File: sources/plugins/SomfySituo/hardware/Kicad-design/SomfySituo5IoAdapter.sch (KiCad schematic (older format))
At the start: 32 parts, among them J1 USB_OTG, J10 Conn_01x01, J11 Conn_01x01, J12 Conn_01x01, J13 Conn_01x01, J14 AVX 00-9188 006, J15 ICSP, J2 Conn_01x01, J3 Conn_01x01, J4 Conn_01x01, J5 Conn_01x01, J6 Conn_01x01, J7 Conn_01x01, J8 Conn_01x01, J9 Conn_01x01, P2 ICSP_PicKit2, U1 FT230X, U2 PIC16F688

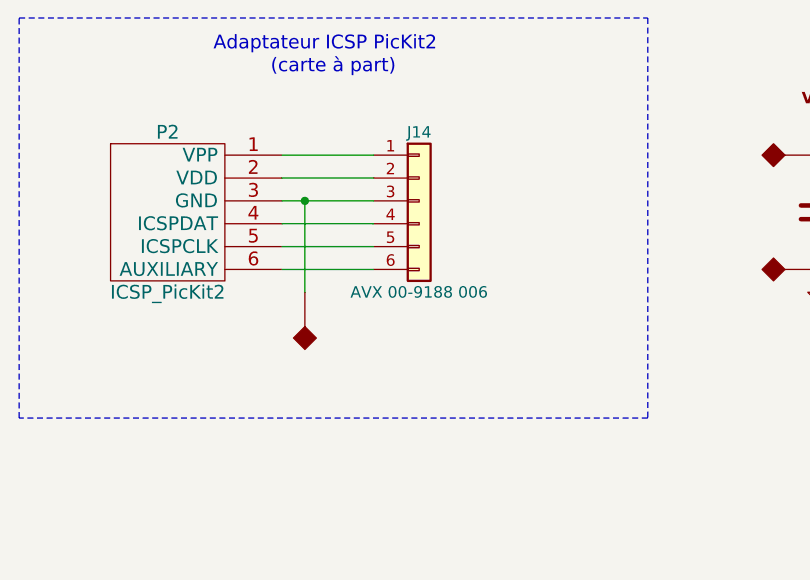
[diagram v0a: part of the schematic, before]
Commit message: Add PicKit2Adapter design (+ PCB)
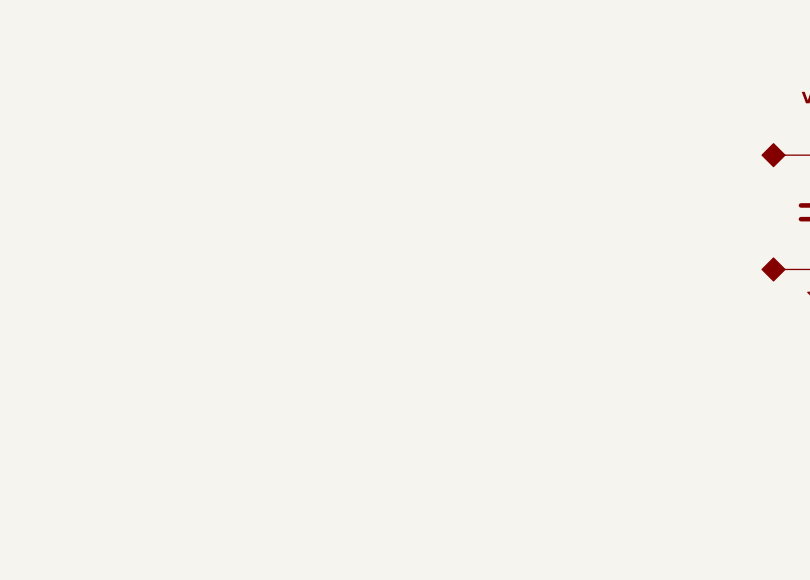
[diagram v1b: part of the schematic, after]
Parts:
- removed J14: AVX 00-9188 006, symbol Conn_01x06
- removed P2: ICSP_PicKit2, Connectors:Wafer_Horizontal17.5x5.8x7RM2.5-6, symbol ICSP_PicKit2
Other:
- note removed: "(carte à part)"
- note removed: "Adaptateur ICSP PicKit2"
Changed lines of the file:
@@
 LIBS:ESD_Protection
 LIBS:CP2102N-A01-GQFN20
-LIBS:ICSP_PicKit2
 LIBS:serial
 LIBS:SomfySituo5IoAdapter-cache
@@
 Text Label 1350 4150 0    60   ~ 0
 VCC_IN
-$Comp
-L ICSP_PicKit2 P2
-U 1 1 5AAA85AF
-P 1600 1850
-F 0 "P2" H 1450 2200 60  0000 C CNN
-F 1 "ICSP_PicKit2" H 1450 1500 60  0000 C CNN
-F 2 "Connectors:Wafer_Horizontal17.5x5.8x7RM2.5-6" H 1600 1850 60  0001 C CNN
-F 3 "" H 1600 1850 60  0001 C CNN
-	1    1600 1850
-	1    0    0    -1
-$EndComp
-Text Notes 1650 1150 0    60   ~ 0
-Adaptateur ICSP PicKit2
-Text Notes 1900 1250 0    60   ~ 0
-(carte à part)
-$Comp
-L Conn_01x06 J14
-U 1 1 5AAA8FB8
-P 2550 1800
-F 0 "J14" H 2550 2100 50  0000 C CNN
-F 1 "AVX 00-9188 006" H 2550 1400 50  0000 C CNN
-F 2 "" H 2550 1800 50  0001 C CNN
-F 3 "" H 2550 1800 50  0001 C CNN
-	1    2550 1800
-	1    0    0    -1
-$EndComp
 Wire Wire Line
 	1000 4750 1000 4850
@@
 Wire Wire Line
 	8500 1550 8800 1550
-Wire Notes Line
-	800  1000 3550 1000
-Wire Notes Line
-	3550 1000 3550 2750
-Wire Notes Line
-	3550 2750 800  2750
-Wire Notes Line
-	800  2750 800  1000
-Wire Wire Line
-	1950 1600 2350 1600
-Wire Wire Line
-	2350 1700 1950 1700
-Wire Wire Line
-	1950 1800 2350 1800
-Wire Wire Line
-	2350 1900 1950 1900
-Wire Wire Line
-	1950 2000 2350 2000
-Wire Wire Line
-	2350 2100 1950 2100
-$Comp
-L PWR_FLAG #FLG2
-U 1 1 5AAA9696
-P 2050 2200
-F 0 "#FLG2" H 2050 2500 60  0001 C CNN
-F 1 "PWR_FLAG" H 2050 2150 40  0001 C CNN
-F 2 "" H 1950 2400 60  0001 C CNN
-F 3 "" H 2050 2500 60  0001 C CNN
-	1    2050 2200
-	-1   0    0    1
-$EndComp
-Wire Wire Line
-	2050 2200 2050 1800
-Connection ~ 2050 1800
 $Comp
 L Conn_01x06 J15

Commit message: Place components
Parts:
- J10, J11, J12, J13, J2, J3, J4, J5, J6, J7, J8, J9: footprint Socket_Strips:Socket_Strip_Straight_1x01_Pitch2.54mm -> Measurement_Points:Measurement_Point_Square-SMD-Pad_Big
- J15: footprint (none) -> AVX 00-9188 006 receiver:AVX_00-9188_006_receiver
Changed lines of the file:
@@
 F 0 "J2" H 9100 1450 50  0000 C CNN
 F 1 "Conn_01x01" H 9450 1450 50  0000 C CNN
-F 2 "Socket_Strips:Socket_Strip_Straight_1x01_Pitch2.54mm" H 9000 1450 50  0001 C CNN
+F 2 "Measurement_Points:Measurement_Point_Square-SMD-Pad_Big" H 9000 1450 50  0001 C CNN
 F 3 "" H 9000 1450 50  0001 C CNN
 	1    9000 1450
@@
 F 0 "J3" H 9100 1550 50  0000 C CNN
 F 1 "Conn_01x01" H 9450 1550 50  0000 C CNN
-F 2 "Socket_Strips:Socket_Strip_Straight_1x01_Pitch2.54mm" H 9000 1550 50  0001 C CNN
+F 2 "Measurement_Points:Measurement_Point_Square-SMD-Pad_Big" H 9000 1550 50  0001 C CNN
 F 3 "" H 9000 1550 50  0001 C CNN
 	1    9000 1550
@@
 F 0 "J4" H 9100 1650 50  0000 C CNN
 F 1 "Conn_01x01" H 9450 1650 50  0000 C CNN
-F 2 "Socket_Strips:Socket_Strip_Straight_1x01_Pitch2.54mm" H 9000 1650 50  0001 C CNN
+F 2 "Measurement_Points:Measurement_Point_Square-SMD-Pad_Big" H 9000 1650 50  0001 C CNN
 F 3 "" H 9000 1650 50  0001 C CNN
 	1    9000 1650
@@
 F 0 "J5" H 9100 1750 50  0000 C CNN
 F 1 "Conn_01x01" H 9450 1750 50  0000 C CNN
-F 2 "Socket_Strips:Socket_Strip_Straight_1x01_Pitch2.54mm" H 9000 1750 50  0001 C CNN
+F 2 "Measurement_Points:Measurement_Point_Square-SMD-Pad_Big" H 9000 1750 50  0001 C CNN
 F 3 "" H 9000 1750 50  0001 C CNN
 	1    9000 1750
@@
 F 0 "J6" H 9100 1850 50  0000 C CNN
 F 1 "Conn_01x01" H 9450 1850 50  0000 C CNN
-F 2 "Socket_Strips:Socket_Strip_Straight_1x01_Pitch2.54mm" H 9000 1850 50  0001 C CNN
+F 2 "Measurement_Points:Measurement_Point_Square-SMD-Pad_Big" H 9000 1850 50  0001 C CNN
 F 3 "" H 9000 1850 50  0001 C CNN
 	1    9000 1850
@@
 F 0 "J7" H 9100 1950 50  0000 C CNN
 F 1 "Conn_01x01" H 9450 1950 50  0000 C CNN
-F 2 "Socket_Strips:Socket_Strip_Straight_1x01_Pitch2.54mm" H 9000 1950 50  0001 C CNN
+F 2 "Measurement_Points:Measurement_Point_Square-SMD-Pad_Big" H 9000 1950 50  0001 C CNN
 F 3 "" H 9000 1950 50  0001 C CNN
 	1    9000 1950
@@
 F 0 "J8" H 9100 2050 50  0000 C CNN
 F 1 "Conn_01x01" H 9450 2050 50  0000 C CNN
-F 2 "Socket_Strips:Socket_Strip_Straight_1x01_Pitch2.54mm" H 9000 2050 50  0001 C CNN
+F 2 "Measurement_Points:Measurement_Point_Square-SMD-Pad_Big" H 9000 2050 50  0001 C CNN
 F 3 "" H 9000 2050 50  0001 C CNN
 	1    9000 2050
@@
 F 0 "J9" H 9100 2150 50  0000 C CNN
 F 1 "Conn_01x01" H 9450 2150 50  0000 C CNN
-F 2 "Socket_Strips:Socket_Strip_Straight_1x01_Pitch2.54mm" H 9000 2150 50  0001 C CNN
+F 2 "Measurement_Points:Measurement_Point_Square-SMD-Pad_Big" H 9000 2150 50  0001 C CNN
 F 3 "" H 9000 2150 50  0001 C CNN
 	1    9000 2150
@@
 F 0 "J10" H 9100 2250 50  0000 C CNN
 F 1 "Conn_01x01" H 9450 2250 50  0000 C CNN
-F 2 "Socket_Strips:Socket_Strip_Straight_1x01_Pitch2.54mm" H 9000 2250 50  0001 C CNN
+F 2 "Measurement_Points:Measurement_Point_Square-SMD-Pad_Big" H 9000 2250 50  0001 C CNN
 F 3 "" H 9000 2250 50  0001 C CNN
 	1    9000 2250
@@
 F 0 "J11" H 9100 2350 50  0000 C CNN
 F 1 "Conn_01x01" H 9450 2350 50  0000 C CNN
-F 2 "Socket_Strips:Socket_Strip_Straight_1x01_Pitch2.54mm" H 9000 2350 50  0001 C CNN
+F 2 "Measurement_Points:Measurement_Point_Square-SMD-Pad_Big" H 9000 2350 50  0001 C CNN
 F 3 "" H 9000 2350 50  0001 C CNN
 	1    9000 2350
@@
 F 0 "J12" H 9100 2450 50  0000 C CNN
 F 1 "Conn_01x01" H 9450 2450 50  0000 C CNN
-F 2 "Socket_Strips:Socket_Strip_Straight_1x01_Pitch2.54mm" H 9000 2450 50  0001 C CNN
+F 2 "Measurement_Points:Measurement_Point_Square-SMD-Pad_Big" H 9000 2450 50  0001 C CNN
 F 3 "" H 9000 2450 50  0001 C CNN
 	1    9000 2450
@@
 $EndComp
 $Comp
-L PWR_FLAG #FLG4
+L PWR_FLAG #FLG3
 U 1 1 5A8F0A07
 P 4300 2100
-F 0 "#FLG4" H 4300 2400 60  0001 C CNN
+F 0 "#FLG3" H 4300 2400 60  0001 C CNN
 F 1 "PWR_FLAG" H 4300 2050 40  0001 C CNN
 F 2 "" H 4200 2300 60  0001 C CNN
@@
 F 0 "J13" H 9100 2550 50  0000 C CNN
 F 1 "Conn_01x01" H 9450 2550 50  0000 C CNN
-F 2 "Socket_Strips:Socket_Strip_Straight_1x01_Pitch2.54mm" H 9000 2550 50  0001 C CNN
+F 2 "Measurement_Points:Measurement_Point_Square-SMD-Pad_Big" H 9000 2550 50  0001 C CNN
 F 3 "" H 9000 2550 50  0001 C CNN
 	1    9000 2550
@@
 F 0 "J15" H 6200 2100 50  0000 C CNN
 F 1 "ICSP" H 6200 1400 50  0000 C CNN
-F 2 "" H 6200 1800 50  0001 C CNN
+F 2 "AVX 00-9188 006 receiver:AVX_00-9188_006_receiver" H 6200 1800 50  0001 C CNN
 F 3 "" H 6200 1800 50  0001 C CNN
 	1    6200 1800
@@
 $EndComp
 $Comp
-L PWR_FLAG #FLG3
+L PWR_FLAG #FLG2
 U 1 1 5AAA9CFB
 P 4300 1600
-F 0 "#FLG3" H 4300 1900 60  0001 C CNN
+F 0 "#FLG2" H 4300 1900 60  0001 C CNN
 F 1 "PWR_FLAG" H 4300 1550 40  0001 C CNN
 F 2 "" H 4200 1800 60  0001 C CNN

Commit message: Finish PCB
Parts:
- J10, J11, J12, J13, J2, J3, J4, J5, J6, J7, J8, J9: footprint Measurement_Points:Measurement_Point_Square-SMD-Pad_Big -> Measurement_Points:Measurement_Point_Square-SMD-Pad_Small
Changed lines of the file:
@@
 F 0 "J2" H 9100 1450 50  0000 C CNN
 F 1 "Conn_01x01" H 9450 1450 50  0000 C CNN
-F 2 "Measurement_Points:Measurement_Point_Square-SMD-Pad_Big" H 9000 1450 50  0001 C CNN
+F 2 "Measurement_Points:Measurement_Point_Square-SMD-Pad_Small" H 9000 1450 50  0001 C CNN
 F 3 "" H 9000 1450 50  0001 C CNN
 	1    9000 1450
@@
 F 0 "J3" H 9100 1550 50  0000 C CNN
 F 1 "Conn_01x01" H 9450 1550 50  0000 C CNN
-F 2 "Measurement_Points:Measurement_Point_Square-SMD-Pad_Big" H 9000 1550 50  0001 C CNN
+F 2 "Measurement_Points:Measurement_Point_Square-SMD-Pad_Small" H 9000 1550 50  0001 C CNN
 F 3 "" H 9000 1550 50  0001 C CNN
 	1    9000 1550
@@
 F 0 "J4" H 9100 1650 50  0000 C CNN
 F 1 "Conn_01x01" H 9450 1650 50  0000 C CNN
-F 2 "Measurement_Points:Measurement_Point_Square-SMD-Pad_Big" H 9000 1650 50  0001 C CNN
+F 2 "Measurement_Points:Measurement_Point_Square-SMD-Pad_Small" H 9000 1650 50  0001 C CNN
 F 3 "" H 9000 1650 50  0001 C CNN
 	1    9000 1650
@@
 F 0 "J5" H 9100 1750 50  0000 C CNN
 F 1 "Conn_01x01" H 9450 1750 50  0000 C CNN
-F 2 "Measurement_Points:Measurement_Point_Square-SMD-Pad_Big" H 9000 1750 50  0001 C CNN
+F 2 "Measurement_Points:Measurement_Point_Square-SMD-Pad_Small" H 9000 1750 50  0001 C CNN
 F 3 "" H 9000 1750 50  0001 C CNN
 	1    9000 1750
@@
 F 0 "J6" H 9100 1850 50  0000 C CNN
 F 1 "Conn_01x01" H 9450 1850 50  0000 C CNN
-F 2 "Measurement_Points:Measurement_Point_Square-SMD-Pad_Big" H 9000 1850 50  0001 C CNN
+F 2 "Measurement_Points:Measurement_Point_Square-SMD-Pad_Small" H 9000 1850 50  0001 C CNN
 F 3 "" H 9000 1850 50  0001 C CNN
 	1    9000 1850
@@
 F 0 "J7" H 9100 1950 50  0000 C CNN
 F 1 "Conn_01x01" H 9450 1950 50  0000 C CNN
-F 2 "Measurement_Points:Measurement_Point_Square-SMD-Pad_Big" H 9000 1950 50  0001 C CNN
+F 2 "Measurement_Points:Measurement_Point_Square-SMD-Pad_Small" H 9000 1950 50  0001 C CNN
 F 3 "" H 9000 1950 50  0001 C CNN
 	1    9000 1950
@@
 F 0 "J8" H 9100 2050 50  0000 C CNN
 F 1 "Conn_01x01" H 9450 2050 50  0000 C CNN
-F 2 "Measurement_Points:Measurement_Point_Square-SMD-Pad_Big" H 9000 2050 50  0001 C CNN
+F 2 "Measurement_Points:Measurement_Point_Square-SMD-Pad_Small" H 9000 2050 50  0001 C CNN
 F 3 "" H 9000 2050 50  0001 C CNN
 	1    9000 2050
@@
 F 0 "J9" H 9100 2150 50  0000 C CNN
 F 1 "Conn_01x01" H 9450 2150 50  0000 C CNN
-F 2 "Measurement_Points:Measurement_Point_Square-SMD-Pad_Big" H 9000 2150 50  0001 C CNN
+F 2 "Measurement_Points:Measurement_Point_Square-SMD-Pad_Small" H 9000 2150 50  0001 C CNN
 F 3 "" H 9000 2150 50  0001 C CNN
 	1    9000 2150
@@
 F 0 "J10" H 9100 2250 50  0000 C CNN
 F 1 "Conn_01x01" H 9450 2250 50  0000 C CNN
-F 2 "Measurement_Points:Measurement_Point_Square-SMD-Pad_Big" H 9000 2250 50  0001 C CNN
+F 2 "Measurement_Points:Measurement_Point_Square-SMD-Pad_Small" H 9000 2250 50  0001 C CNN
 F 3 "" H 9000 2250 50  0001 C CNN
 	1    9000 2250
@@
 F 0 "J11" H 9100 2350 50  0000 C CNN
 F 1 "Conn_01x01" H 9450 2350 50  0000 C CNN
-F 2 "Measurement_Points:Measurement_Point_Square-SMD-Pad_Big" H 9000 2350 50  0001 C CNN
+F 2 "Measurement_Points:Measurement_Point_Square-SMD-Pad_Small" H 9000 2350 50  0001 C CNN
 F 3 "" H 9000 2350 50  0001 C CNN
 	1    9000 2350
@@
 F 0 "J12" H 9100 2450 50  0000 C CNN
 F 1 "Conn_01x01" H 9450 2450 50  0000 C CNN
-F 2 "Measurement_Points:Measurement_Point_Square-SMD-Pad_Big" H 9000 2450 50  0001 C CNN
+F 2 "Measurement_Points:Measurement_Point_Square-SMD-Pad_Small" H 9000 2450 50  0001 C CNN
 F 3 "" H 9000 2450 50  0001 C CNN
 	1    9000 2450
@@
 F 0 "J13" H 9100 2550 50  0000 C CNN
 F 1 "Conn_01x01" H 9450 2550 50  0000 C CNN
-F 2 "Measurement_Points:Measurement_Point_Square-SMD-Pad_Big" H 9000 2550 50  0001 C CNN
+F 2 "Measurement_Points:Measurement_Point_Square-SMD-Pad_Small" H 9000 2550 50  0001 C CNN
 F 3 "" H 9000 2550 50  0001 C CNN
 	1    9000 2550

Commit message: Update USB connector footprint
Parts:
- J1: footprint Connectors:USB_Micro-B -> USB_Micro-B_AC0002646:USB_Micro-B_AC0002646
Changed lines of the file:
@@
 F 0 "J1" H 800 4800 50  0000 L CNN
 F 1 "USB_OTG" H 800 4700 50  0000 L CNN
-F 2 "Connectors:USB_Micro-B" H 1150 4300 50  0001 C CNN
+F 2 "USB_Micro-B_AC0002646:USB_Micro-B_AC0002646" H 1150 4300 50  0001 C CNN
 F 3 "" H 1150 4300 50  0001 C CNN
 	1    1000 4350
